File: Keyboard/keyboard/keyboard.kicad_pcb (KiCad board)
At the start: 2 copper layers, 158.5 x 70 mm, 57 parts, among them J1 Conn_01x05_Male, J2 Conn_01x06_Male, J3 Conn_01x06_Male, M3 MountingHole_3.2mm_M3, SW1 SW_Push, SW10 Cherry_MX_1u, SW11 Cherry_MX_1u, SW12 Cherry_MX_1u, SW13 Cherry_MX_1u, SW2 Cherry_MX_1u, SW3 Cherry_MX_1u, SW4 Cherry_MX_1u, SW5 Cherry_MX_1u, SW6 Cherry_MX_1u, SW7 Cherry_MX_1u, SW8 Cherry_MX_1u, SW9 Cherry_MX_1u, U1 STM32G030K6T6, U2 LMR62421XMF

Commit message: pcb design fixing
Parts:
- removed C3: 100nF, Capacitor_SMD:C_0805_2012Metric_Pad1.18x1.45mm_HandSolder
- removed D10, D11, D12, D3, D4, D5, D6, D7, D8, D9: LL4148, Diode_SMD:D_MiniMELF
- removed D14: GREEN LED, LED_SMD:LED_0805_2012Metric_Pad1.15x1.40mm_HandSolder
- removed D15: RED LED, LED_SMD:LED_0805_2012Metric_Pad1.15x1.40mm_HandSolder
- removed M3 (x4): MountingHole_3.2mm_M3, MountingHole:MountingHole_3.2mm_M3
- added J4: Conn_01x10_Male, Connector_IDC:IDC-Header_2x05_P2.54mm_Horizontal, F.Cu at (197.2, 75.7)
- added R11: 100, Resistor_SMD:R_0805_2012Metric_Pad1.20x1.40mm_HandSolder, B.Cu at (117.0, 91.4)
- added R12: 100, Resistor_SMD:R_0805_2012Metric_Pad1.20x1.40mm_HandSolder, B.Cu at (128.0, 58.9)
- added R13: 10K, Resistor_SMD:R_0805_2012Metric_Pad1.20x1.40mm_HandSolder, B.Cu at (95.9, 96.2)
- added R14: 10K, Resistor_SMD:R_0805_2012Metric_Pad1.20x1.40mm_HandSolder, B.Cu at (155.0, 57.9)
- added R15: 100, Resistor_SMD:R_0805_2012Metric_Pad1.20x1.40mm_HandSolder, B.Cu at (151.5, 58.9)
- added R16: 100, Resistor_SMD:R_0805_2012Metric_Pad1.20x1.40mm_HandSolder, B.Cu at (94.9, 91.4)
- added R17: 10K, Resistor_SMD:R_0805_2012Metric_Pad1.20x1.40mm_HandSolder, B.Cu at (73.0, 96.5)
- added R18: 10K, Resistor_SMD:R_0805_2012Metric_Pad1.20x1.40mm_HandSolder, B.Cu at (179.3, 58.0)
- added R19: 100, Resistor_SMD:R_0805_2012Metric_Pad1.20x1.40mm_HandSolder, B.Cu at (72.0, 91.4)
- added R20: 100, Resistor_SMD:R_0805_2012Metric_Pad1.20x1.40mm_HandSolder, B.Cu at (174.7, 58.9)
- added R21: 10K, Resistor_SMD:R_0805_2012Metric_Pad1.20x1.40mm_HandSolder, B.Cu at (65.0, 57.8)
- added R22: 10K, Resistor_SMD:R_0805_2012Metric_Pad1.20x1.40mm_HandSolder, B.Cu at (193.2, 54.4)
- added R23: 100, Resistor_SMD:R_0805_2012Metric_Pad1.20x1.40mm_HandSolder, B.Cu at (60.7, 58.8)
- added R24: 100, Resistor_SMD:R_0805_2012Metric_Pad1.20x1.40mm_HandSolder, B.Cu at (196.6, 57.1)
- added R25: 10K, Resistor_SMD:R_0805_2012Metric_Pad1.20x1.40mm_HandSolder, B.Cu at (86.6, 57.7)
- added R26: 10K, Resistor_SMD:R_0805_2012Metric_Pad1.20x1.40mm_HandSolder, B.Cu at (168.2, 88.6)
- added R27: 100, Resistor_SMD:R_0805_2012Metric_Pad1.20x1.40mm_HandSolder, B.Cu at (83.0, 58.9)
- added R28: 100, Resistor_SMD:R_0805_2012Metric_Pad1.20x1.40mm_HandSolder, B.Cu at (176.4, 89.6)
- added R29: 10K, Resistor_SMD:R_0805_2012Metric_Pad1.20x1.40mm_HandSolder, B.Cu at (110.5, 57.5)
- added R30: 10K, Resistor_SMD:R_0805_2012Metric_Pad1.20x1.40mm_HandSolder, B.Cu at (162.5, 88.1)
- added R31: 100, Resistor_SMD:R_0805_2012Metric_Pad1.20x1.40mm_HandSolder, B.Cu at (106.6, 58.9)
- added R32: 100, Resistor_SMD:R_0805_2012Metric_Pad1.20x1.40mm_HandSolder, B.Cu at (153.8, 88.1)
- D1: value LL4148 -> GREEN LED; footprint Diode_SMD:D_MiniMELF -> LED_SMD:LED_0805_2012Metric_Pad1.15x1.40mm_HandSolder
- D2: value LL4148 -> RED LED; footprint Diode_SMD:D_MiniMELF -> LED_SMD:LED_0805_2012Metric_Pad1.15x1.40mm_HandSolder
- J2: value Conn_01x06_Male -> Conn_01x10_Male; footprint Connector_PinSocket_2.54mm:PinSocket_1x06_P2.54mm_Vertical -> Connector_IDC:IDC-Header_2x05_P2.54mm_Horizontal; moved to B.Cu
- J3: value Conn_01x06_Male -> Conn_01x10_Male; footprint Connector_PinSocket_2.54mm:PinSocket_1x06_P2.54mm_Vertical -> Connector_IDC:IDC-Header_2x05_P2.54mm_Horizontal
- R10, R9: value 1k -> 10K; moved to B.Cu
- R3, R4: value 10K -> 1k
- R5: value 100k -> 10k
- moved D1 85.8 mm to (193.0, 89.9), turned to -90 degrees
- moved D2 83.7 mm to (192.6, 108.3), turned to 90 degrees
- moved R4 75.6 mm to (189.0, 106.3)
- moved R10 74.8 mm to (131.7, 58.0), turned to 90 degrees
- moved R9 73.5 mm to (120.3, 93.9)
- moved R3 70.3 mm to (188.9, 89.8)
- moved J2 63.3 mm to (143.0, 108.6), turned to -90 degrees
- moved J3 30.8 mm to (47.9, 108.4), turned to 180 degrees
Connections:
- D1 pad 1: KSWC1k -> GND
- D2 pad 1: KSWC7k -> GND
- J2 pad 1: I2C1_SCL -> LOAD
- J2 pad 2: I2C1_SDA -> GND
- J2 pad 3: I2C2_SDAk -> LOAD
- J2 pad 4: I2C2_SCLk -> GND
- J2 pad 5: LOAD -> I2C1_SDA
- J3 pad 1: I2C1_SCL -> GND
- J3 pad 2: I2C1_SDA -> GND
- J3 pad 4: I2C2_SCLk -> GND
- J3 pad 5: LOAD -> I2C2_SCLk
- R10 pad 1: USART1_TXk -> KSWC7k
- R10 pad 2: Net-(D15-Pad2) -> +3V3
- R3 pad 1: KSWR1k -> LOAD
- R3 pad 2: +3V3 -> Net-(D1-Pad2)
- R4 pad 1: KSWR1k -> STATUS_LEDk
- R4 pad 2: ROW -> Net-(D2-Pad2)
- R9 pad 1: USART1_TXk -> KSWC1k
- R9 pad 2: Net-(D14-Pad1) -> +3V3
- SW10 pad 1: Net-(D9-Pad2) -> GND
- SW10 pad 2: ROW -> Net-(R27-Pad2)
- SW11 pad 1: Net-(D10-Pad2) -> GND
- SW11 pad 2: ROW -> Net-(R28-Pad2)
- SW12 pad 1: Net-(D11-Pad2) -> GND
- SW12 pad 2: ROW -> Net-(R31-Pad2)
- SW13 pad 1: Net-(D12-Pad2) -> GND
- SW13 pad 2: ROW -> Net-(R32-Pad2)
- SW2 pad 1: Net-(D1-Pad2) -> GND
- SW2 pad 2: ROW -> Net-(R11-Pad2)
- SW3 pad 1: Net-(D2-Pad2) -> GND
- SW3 pad 2: ROW -> Net-(R12-Pad2)
- SW4 pad 1: Net-(D3-Pad2) -> GND
- SW4 pad 2: ROW -> Net-(R16-Pad2)
- SW5 pad 1: Net-(D4-Pad2) -> GND
- SW5 pad 2: ROW -> Net-(R15-Pad2)
- SW6 pad 1: Net-(D5-Pad2) -> GND
- SW6 pad 2: ROW -> Net-(R19-Pad2)
- SW7 pad 1: Net-(D6-Pad2) -> GND
- SW7 pad 2: ROW -> Net-(R20-Pad2)
- SW8 pad 1: Net-(D7-Pad2) -> GND
- SW8 pad 2: ROW -> Net-(R23-Pad2)
- SW9 pad 1: Net-(D8-Pad2) -> GND
- SW9 pad 2: ROW -> Net-(R24-Pad2)
- U1 pad 10: KSWC3k -> KSWC4k
- U1 pad 11: KSWC4k -> KSWC5k
- U1 pad 12: KSWC5k -> KSWC6k
- U1 pad 13: KSWC6k -> KSWC7k
- U1 pad 14: KSWC7k -> KSWC8k
- U1 pad 15: KSWC8k -> KSWC9k
- U1 pad 16: KSWC9k -> KSWC10k
- U1 pad 17: KSWC10k -> KSWC11k
- U1 pad 18: KSWC11k -> KSWC12k
- U1 pad 20: KSWC12k -> unconnected-(U1-Pad20)
- U1 pad 30: USART1_TXk -> STATUS_LEDk
- U1 pad 7: KSWR1k -> KSWC1k
- U1 pad 8: KSWC1k -> KSWC2k
- U1 pad 9: KSWC2k -> KSWC3k
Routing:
- net ROW: track 286.1 -> 0.00 mm, vias 2 -> 0
- net +3V3: track 156.8 -> 414.5 mm, vias 8 -> 9
- net I2C1_SDA: track 171.2 -> 33.5 mm, vias 5 -> 3
- net I2C1_SCL: track 171.1 -> 37.3 mm
- net USART1_TXk: track 66.6 -> 0.00 mm, vias 1 -> 0
- net STATUS_LEDk: track 0.00 -> 63.2 mm
- net LOAD: track 168.9 -> 208.5 mm, vias 5 -> 8
- net KSWC10k: track 55.5 -> 90.3 mm
- net KSWC9k: track 34.5 -> 67.5 mm
- net KSWC8k: track 18.4 -> 45.9 mm
- net KSWC12k: track 16.6 -> 35.2 mm
- net KSWR1k: track 12.9 -> 0.00 mm
- net KSWC7k: track 18.4 -> 28.8 mm
- net Net-(D4-Pad2): track 8.95 -> 0.00 mm
- net KSWC3k: track 68.5 -> 60.2 mm
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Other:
- board size 158.5 x 70 mm -> 160.5 x 70 mm

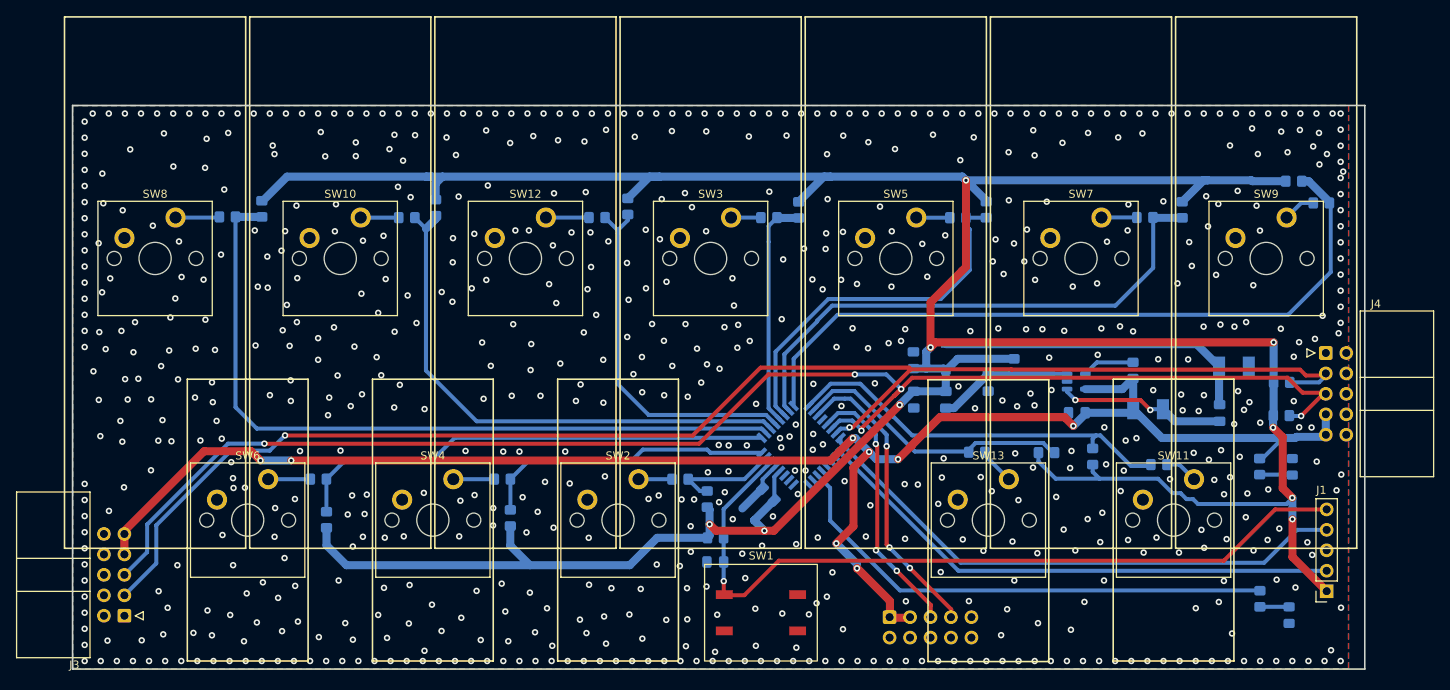
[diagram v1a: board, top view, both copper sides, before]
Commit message: pcb mounting hole change
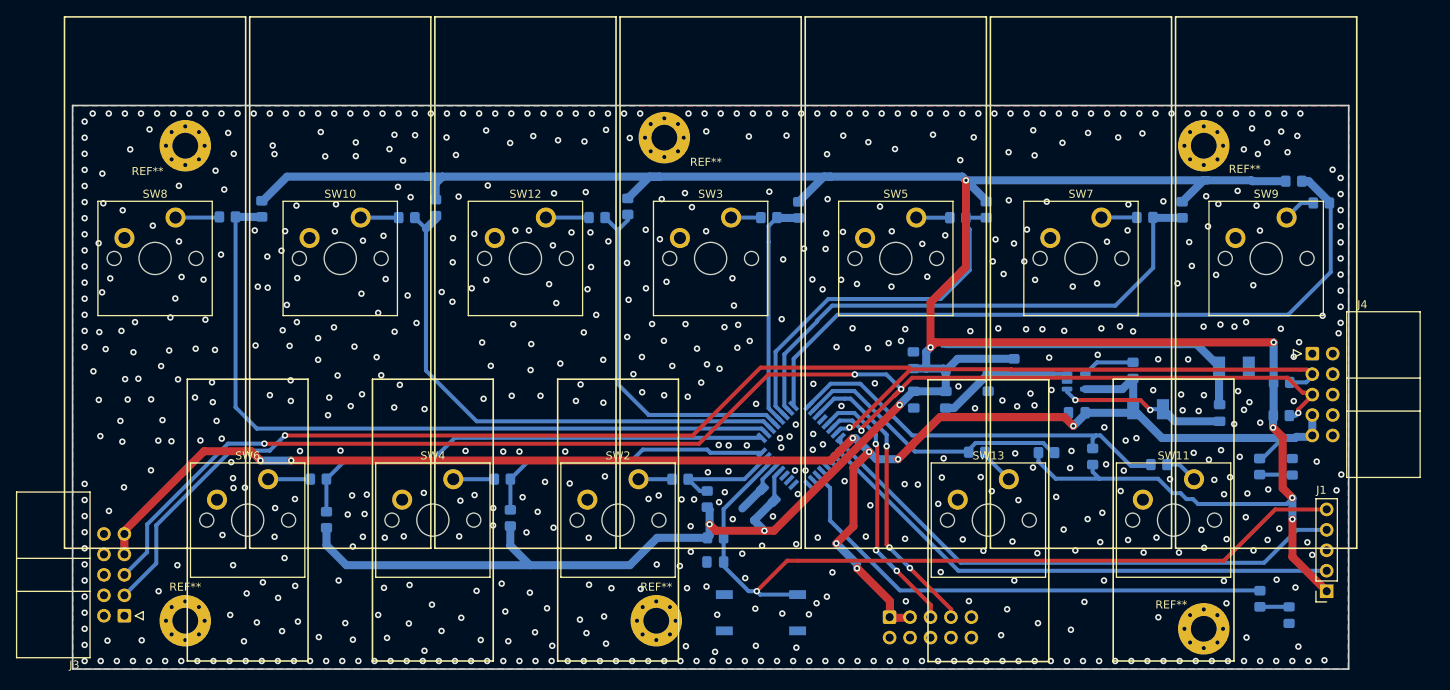
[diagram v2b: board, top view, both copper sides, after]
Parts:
- added REF**: MountingHole_3.2mm_M3_Pad_Via, MountingHole:MountingHole_3.2mm_M3_Pad_Via, F.Cu at (55.5, 50.0)
- added REF**: MountingHole_3.2mm_M3_Pad_Via, MountingHole:MountingHole_3.2mm_M3_Pad_Via, F.Cu at (182.0, 110.0)
- added REF**: MountingHole_3.2mm_M3_Pad_Via, MountingHole:MountingHole_3.2mm_M3_Pad_Via, F.Cu at (114.0, 109.0)
- added REF**: MountingHole_3.2mm_M3_Pad_Via, MountingHole:MountingHole_3.2mm_M3_Pad_Via, F.Cu at (182.0, 50.0)
- added REF**: MountingHole_3.2mm_M3_Pad_Via, MountingHole:MountingHole_3.2mm_M3_Pad_Via, F.Cu at (115.0, 49.0)
- added REF**: MountingHole_3.2mm_M3_Pad_Via, MountingHole:MountingHole_3.2mm_M3_Pad_Via, F.Cu at (55.5, 109.0)
- SW1: moved to B.Cu
- moved J4 1.68 mm to (195.5, 75.8)
- turned SW1 to 180 degrees
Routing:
- net I2C2_SDAk: track 181.6 -> 178.4 mm
- net NRSTk: track 98.3 -> 101.0 mm
- net I2C2_SCLk: track 182.2 -> 179.6 mm
- net LOAD: track 208.5 -> 206.6 mm
- net GND: vias 712 -> 685
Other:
- board size 160.5 x 70 mm -> 158.5 x 70 mm

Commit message: gerber files generated
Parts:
- removed REF** (x6): MountingHole_3.2mm_M3_Pad_Via, MountingHole:MountingHole_3.2mm_M3_Pad_Via
- added H1: MountingHole, MountingHole:MountingHole_3.2mm_M3_Pad_Via, F.Cu at (55.5, 50.0)
- added H2: MountingHole, MountingHole:MountingHole_3.2mm_M3_Pad_Via, F.Cu at (115.0, 49.0)
- added H3: MountingHole, MountingHole:MountingHole_3.2mm_M3_Pad_Via, F.Cu at (182.0, 50.0)
- added H4: MountingHole, MountingHole:MountingHole_3.2mm_M3_Pad_Via, F.Cu at (182.0, 110.0)
- added H5: MountingHole, MountingHole:MountingHole_3.2mm_M3_Pad_Via, F.Cu at (114.0, 109.0)
- added H6: MountingHole, MountingHole:MountingHole_3.2mm_M3_Pad_Via, F.Cu at (55.5, 109.0)
- J3, J4: footprint Connector_IDC:IDC-Header_2x05_P2.54mm_Horizontal -> Connector_IDC:IDC-Header_2x05_P2.54mm_Vertical; moved to B.Cu
- moved J3 10.3 mm to (47.9, 98.1)
- moved J4 10.2 mm to (195.5, 86.0)
- moved R2 3.08 mm to (188.9, 80.7)
- moved R1 2.93 mm to (188.7, 83.2)
- moved D1 2.67 mm to (190.3, 90.0)
- moved R3 1.73 mm to (187.2, 89.9)
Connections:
- J3 pad 1: GND -> LOAD
- J3 pad 3: I2C2_SDAk -> LOAD
- J3 pad 7: LOAD -> I2C2_SDAk
- J3 pad 9: LOAD -> GND
- J4 pad 1: GND -> LOAD
- J4 pad 3: I2C2_SDAk -> LOAD
- J4 pad 7: LOAD -> I2C2_SDAk
- J4 pad 9: LOAD -> GND
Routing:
- net I2C2_SDAk: track 178.4 -> 181.7 mm
- net +3V3: track 414.5 -> 417.7 mm
- net I2C2_SCLk: track 179.6 -> 182.7 mm
- net LOAD: track 206.6 -> 208.4 mm
- net Net-(D1-Pad2): track 4.07 -> 3.23 mm
- net GND: vias 685 -> 693
